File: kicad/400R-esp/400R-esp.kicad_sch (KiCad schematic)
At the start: 23 parts, among them J1 LcdPower, J2 ToEncoder, J32 ToESP, SW1 RotaryEncoder, SW2 SW_Push, U1 ESP32-DEVKITC-32E

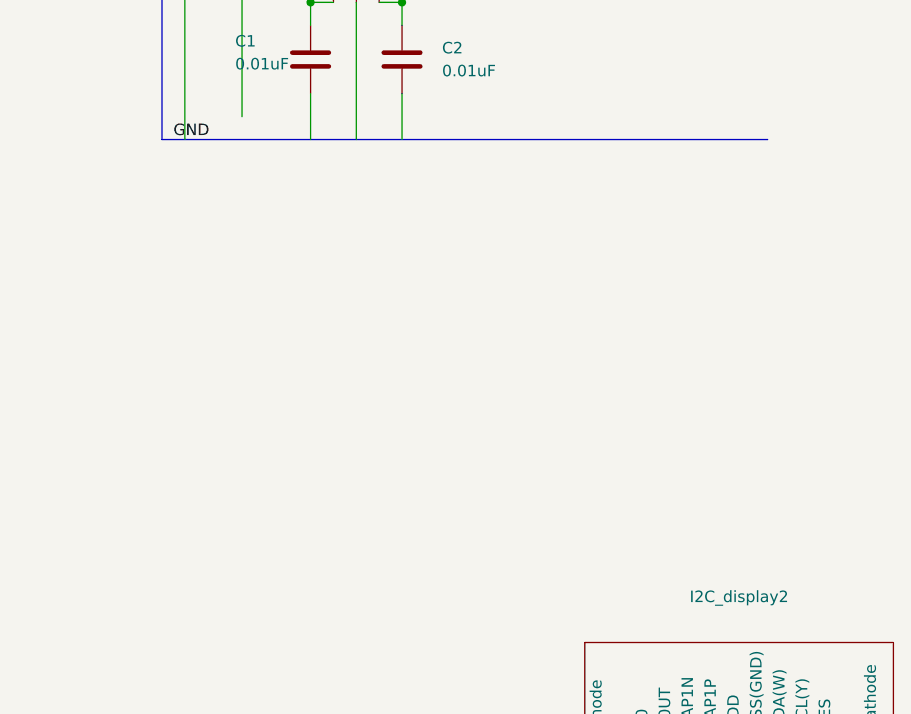
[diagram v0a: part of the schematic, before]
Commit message: partSpecMdとフットライトの現物合わせ修正
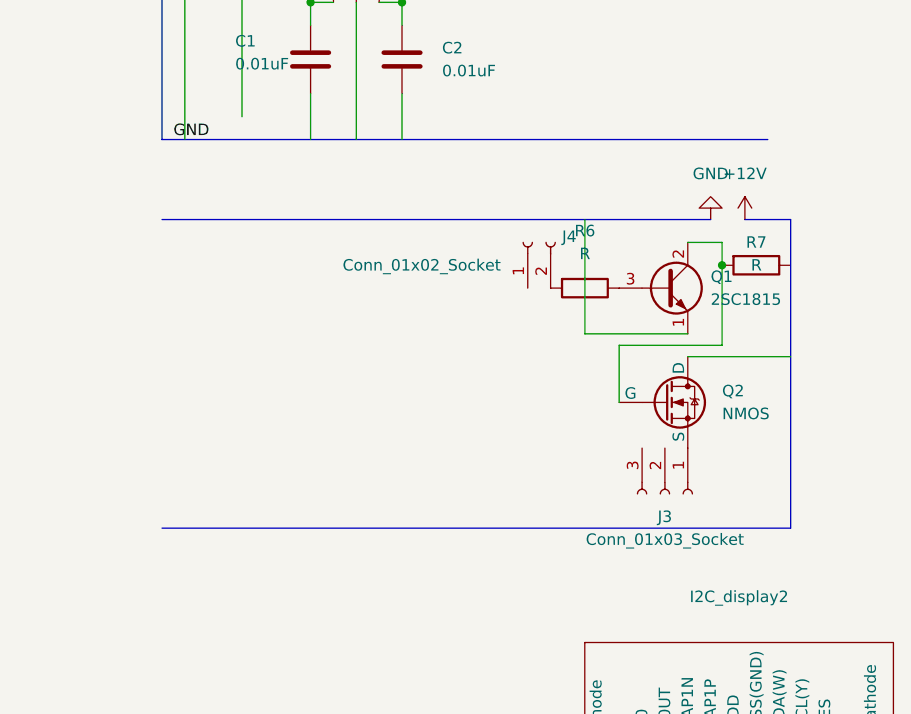
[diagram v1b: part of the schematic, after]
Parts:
- added J3: Conn_01x03_Socket, symbol Connector:Conn_01x03_Socket
- added J4: Conn_01x02_Socket, symbol Connector:Conn_01x02_Socket
- added Q1: 2SC1815, Package_TO_SOT_THT:TO-92_Inline, symbol Transistor_BJT:2SC1815
- added Q2: NMOS, symbol Simulation_SPICE:NMOS
- added R6, R7: R, symbol Device:R
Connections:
- new net: Q1.3 (B), R6.1
- new net: J4.2 (Pin_2), R6.2
- new net: J3.1 (Pin_1), Q2.3 (S)
- new net: Q1.2 (C), Q2.2 (G), R7.2

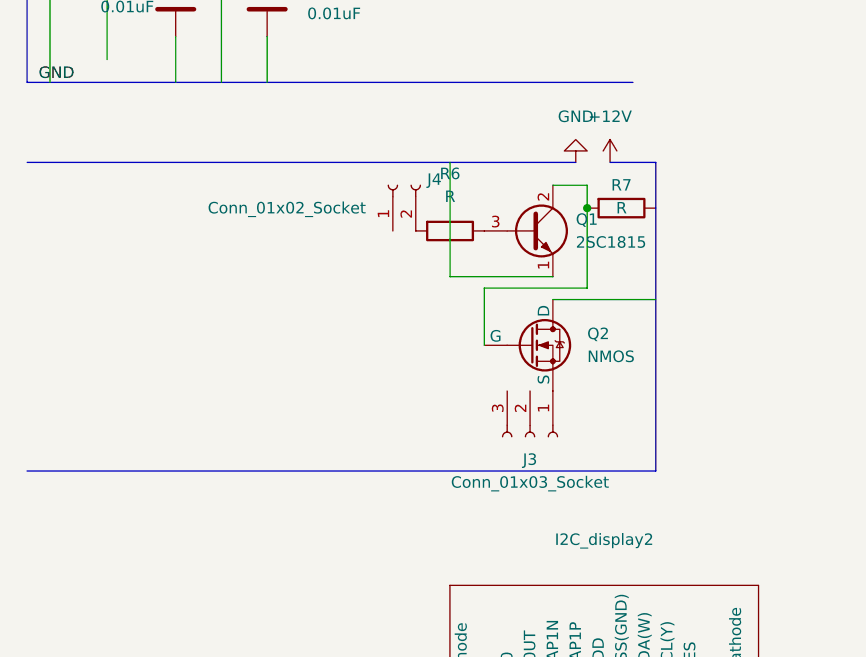
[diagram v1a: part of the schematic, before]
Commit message: イルミ線機能を追加
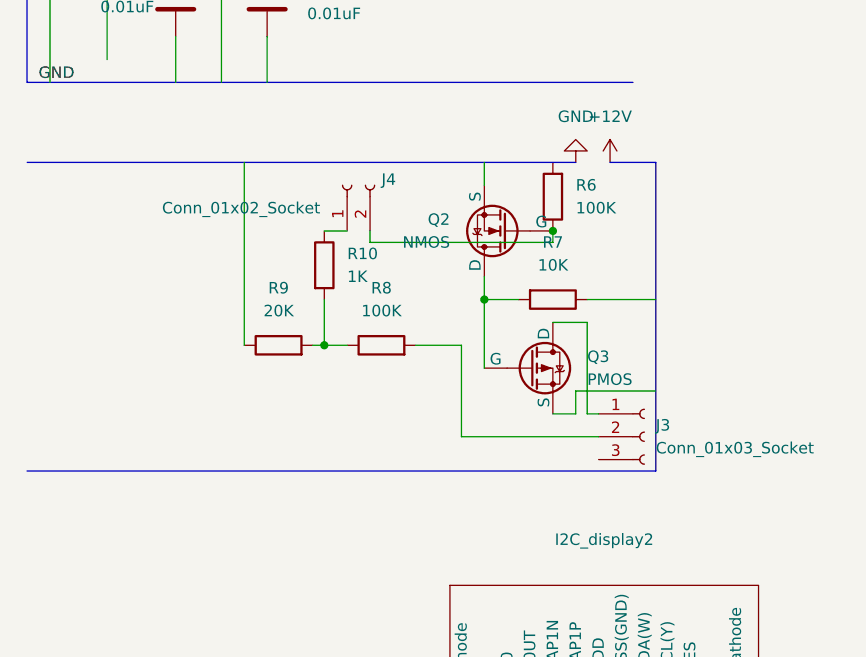
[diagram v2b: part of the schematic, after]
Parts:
- removed Q1: 2SC1815, Package_TO_SOT_THT:TO-92_Inline, symbol Transistor_BJT:2SC1815
- added Q3: PMOS, symbol Simulation_SPICE:PMOS
- added R10: 1K, symbol Device:R
- added R8: 100K, symbol Device:R
- added R9: 20K, symbol Device:R
- R6: value R -> 100K
- R7: value R -> 10K
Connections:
- net at R6.1: now also J4.2 (Pin_2), Q2.2 (G)
- net at R6.2: no longer J4.2 (Pin_2)
- net at J3.1 (Pin_1): now also Q3.1 (D); no longer Q2.3 (S)
- net at J3.2 (Pin_2): now also R8.2
- net at J4.1 (Pin_1): now also R10.1
- net at R7.2: now also Q2.1 (D), Q3.2 (G); no longer Q2.2 (G)
- new net: R10.2, R8.1, R9.2
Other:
- moved on the sheet: J3, J4, Q2, R6

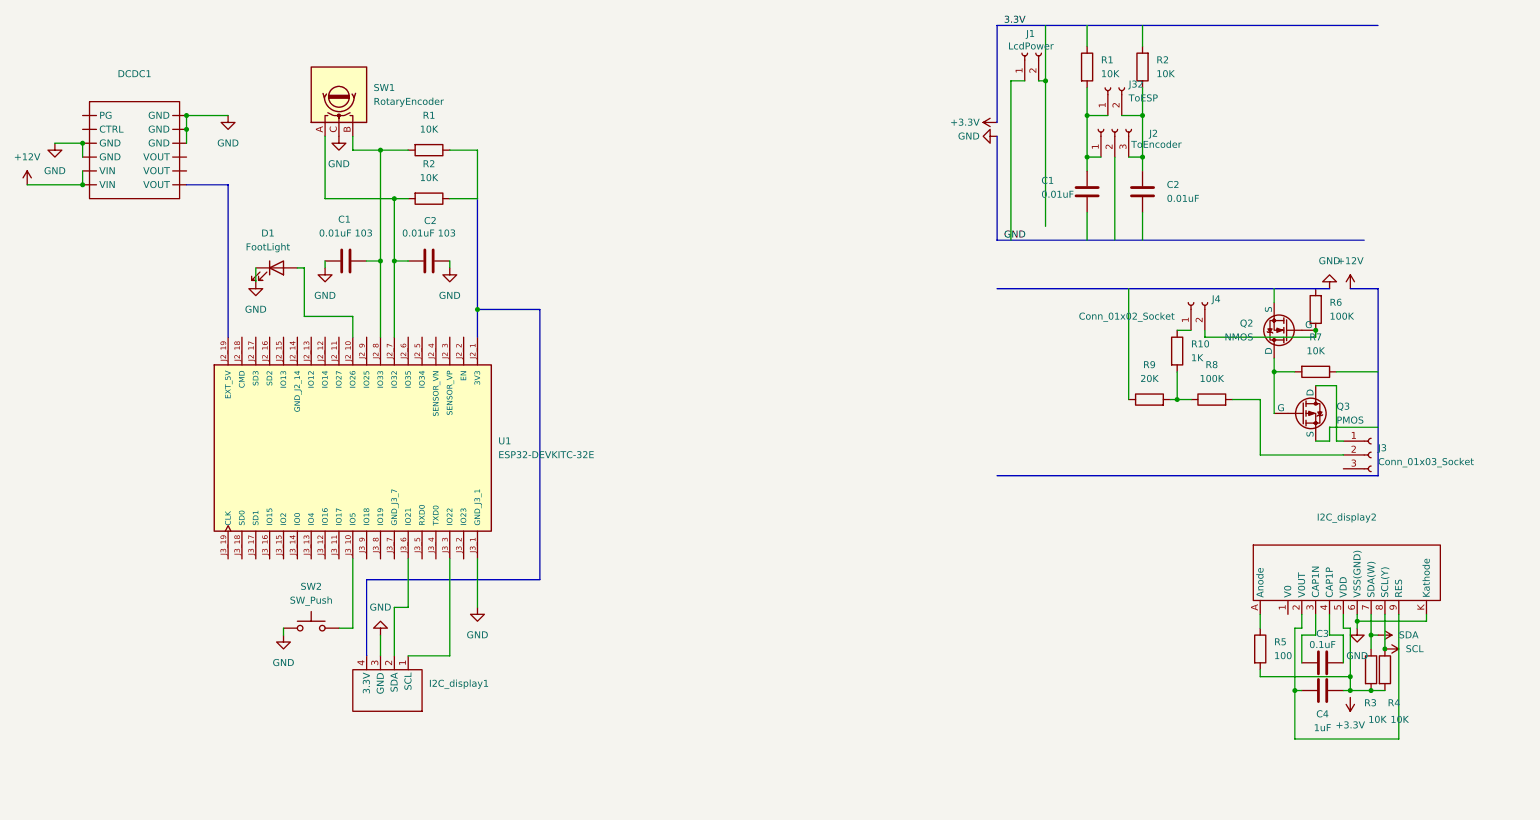
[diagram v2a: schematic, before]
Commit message: ハートライトとサイドブレーキ機能追加(変更機能未了)
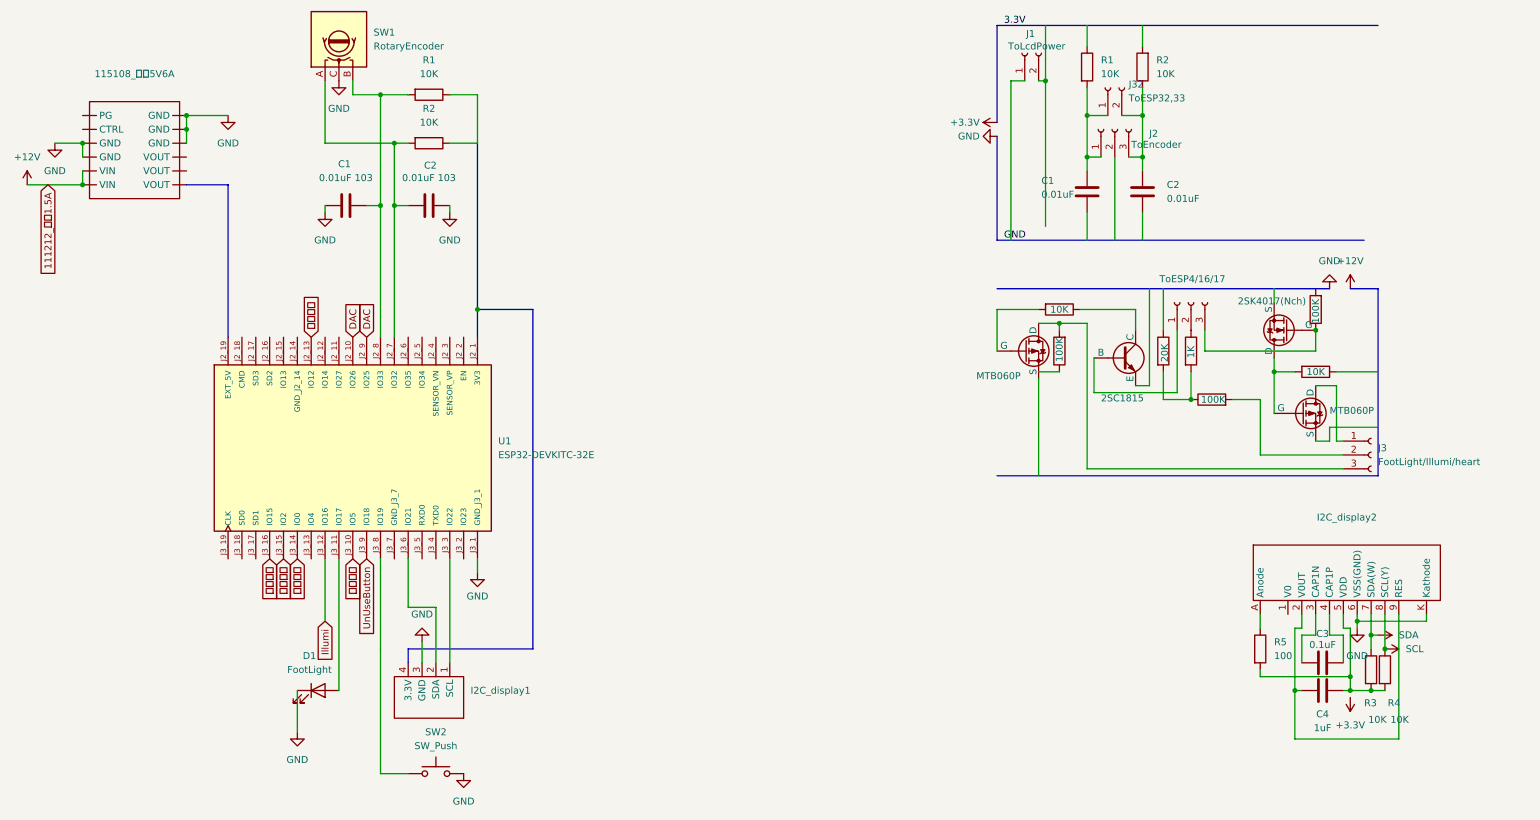
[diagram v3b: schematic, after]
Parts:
- removed J4: Conn_01x02_Socket, symbol Connector:Conn_01x02_Socket
- added J5: ToESP4/16/17, symbol Connector:Conn_01x03_Socket
- added Q1: 2SC1815, Package_TO_SOT_THT:TO-92_Inline, symbol Transistor_BJT:2SC1815
- added Q4: MTB060P, symbol Simulation_SPICE:PMOS
- added R11: 100K, symbol Device:R
- added R12: 10K, symbol Device:R
- J1: value LcdPower -> ToLcdPower
- J3: value Conn_01x03_Socket -> FootLight/Illumi/heart
- J32: value ToESP -> ToESP32,33
- Q2: value NMOS -> 2SK4017(Nch)
- Q3: value PMOS -> MTB060P
- renumbered DCDC1 to 115108_出力5V6A
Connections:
- net GND: now also SW2.2; no longer SW2.1
- net at Q2.2 (G), R6.1: now also J5.3 (Pin_3)
- net at J3.3 (Pin_3): now also Q4.1 (D), R11.2
- net at R10.1: now also J5.2 (Pin_2)
- net 使用不可: now reaches U1.J3_10 (IO5)
- net 使用不可: now also U1.J2_13 (IO12), U1.J3_14 (IO0), U1.J3_15 (IO2), U1.J3_16 (IO15); no longer SW2.2
- net at D1.2 (A): now also U1.J3_11 (IO17); no longer U1.J2_10 (IO26)
- net DAC: now reaches U1.J2_9 (IO25)
- net DAC: now also U1.J2_10 (IO26)
- net Illumi: now reaches U1.J3_12 (IO16)
- net at U1.J3_8 (IO19): now also SW2.1
- net UnUseButton: now reaches U1.J3_9 (IO18)
- new net: J5.1 (Pin_1), Q1.3 (B)
- new net: Q4.2 (G), R12.2
- new net: Q1.2 (C), R12.1
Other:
- moved on the sheet: C1, C2, D1, I2C_display1, R1, R2, SW1, SW2
